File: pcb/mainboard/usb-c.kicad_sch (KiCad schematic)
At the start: 4 parts

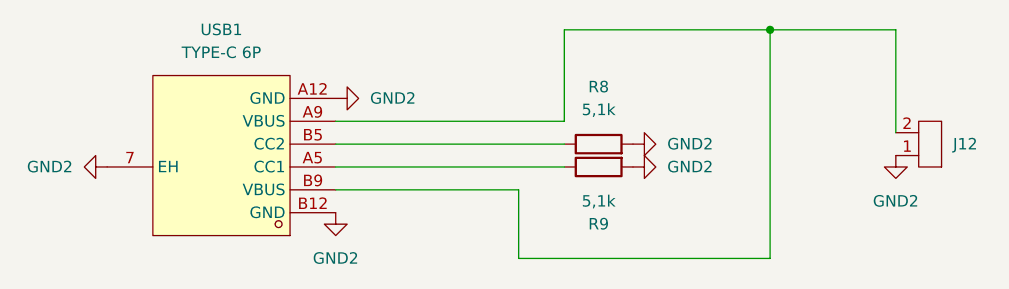
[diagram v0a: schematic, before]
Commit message: making separate pcbs
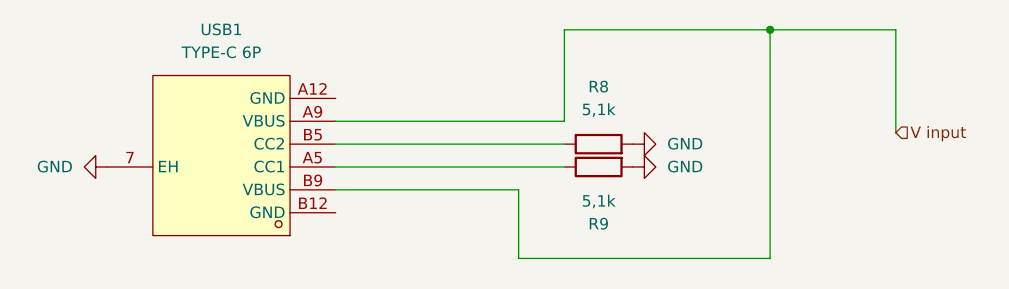
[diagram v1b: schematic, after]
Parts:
- removed J12: (no value), Library:copper_pad 2x, symbol New_Library:copper_pad_2x
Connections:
- net V input: now reaches USB1.A9 (VBUS), USB1.B9 (VBUS)
- net GND2 renamed GND
- net GND: no longer USB1.A12 (GND), USB1.B12 (GND)
